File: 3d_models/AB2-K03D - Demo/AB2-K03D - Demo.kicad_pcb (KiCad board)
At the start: 2 copper layers, 209 parts

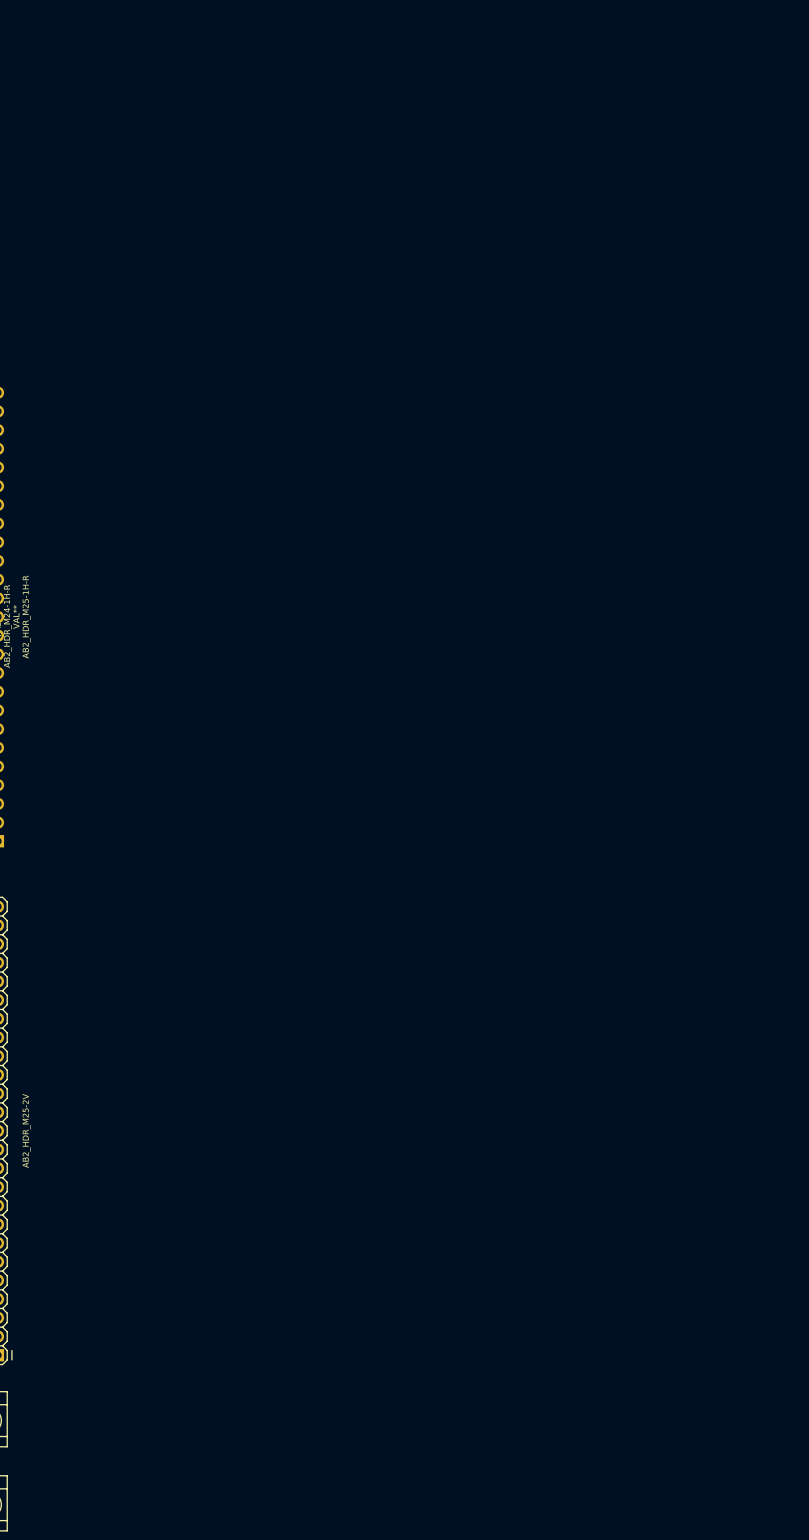
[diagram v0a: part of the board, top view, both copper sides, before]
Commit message: AB2-K03D: add FR4 substrates
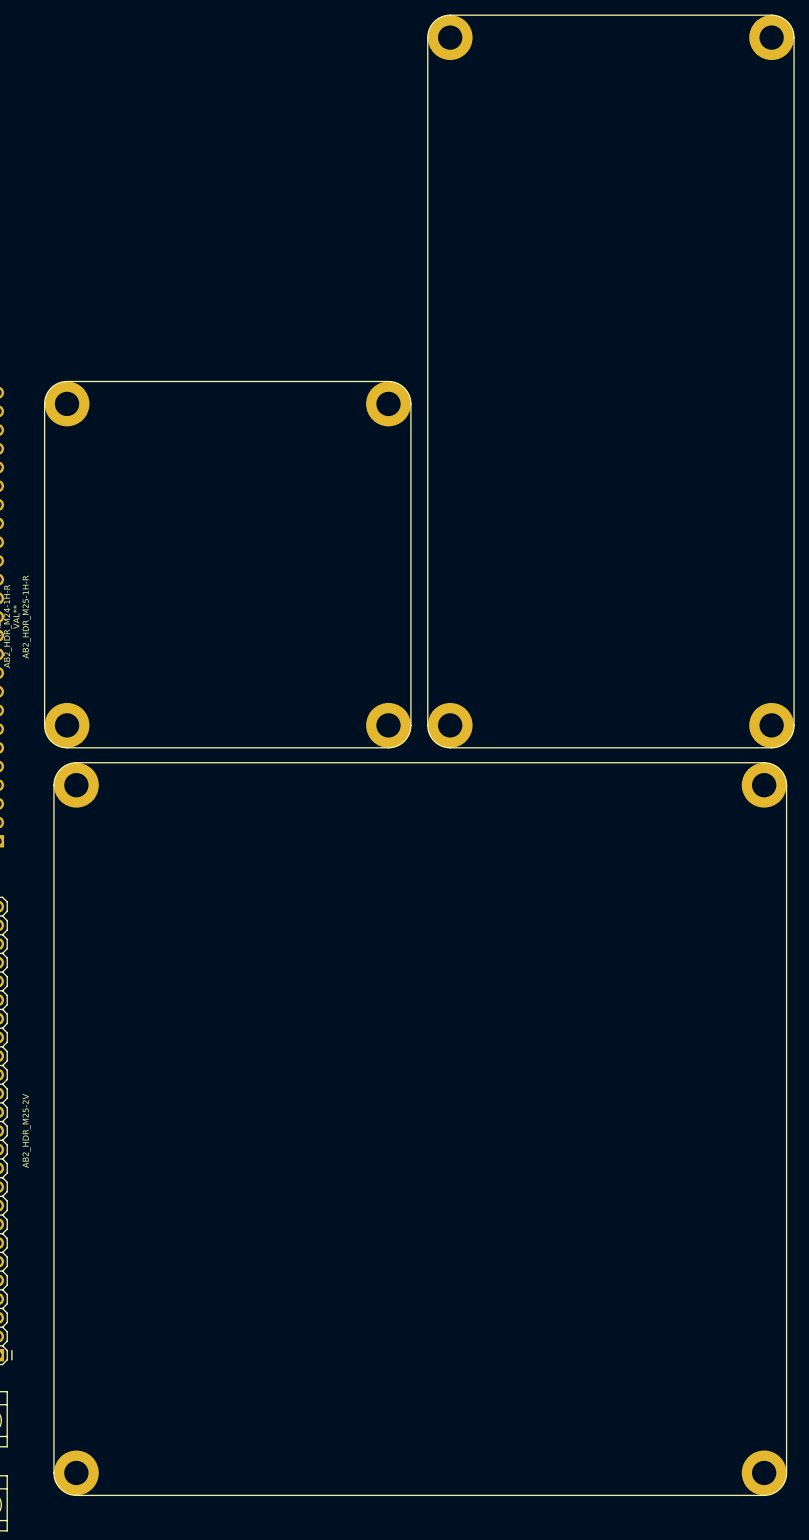
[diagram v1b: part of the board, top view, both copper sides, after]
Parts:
- added AB2_STANDOFF_1.96x1.96_BOARD_ROUNDED_CORNERS_KEEPOUT_FR4: VAL**, AB2_STANDOFF_1.96x1.96_BOARD_ROUNDED_CORNERS_KEEPOUT_FR4, F.Cu at (304.8, 166.4)
- added AB2_STANDOFF_1.96x3.92_BOARD_ROUNDED_CORNERS_KEEPOUT_FR4: VAL**, AB2_STANDOFF_1.96x3.92_BOARD_ROUNDED_CORNERS_KEEPOUT_FR4, F.Cu at (356.9, 166.4)
- added AB2_STANDOFF_3.92x3.92_BOARD_ROUNDED_CORNERS_KEEPOUT_FR4: VAL**, AB2_STANDOFF_3.92x3.92_BOARD_ROUNDED_CORNERS_KEEPOUT_FR4, F.Cu at (306.1, 268.0)
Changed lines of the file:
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@@
     (tracks 0)
     (zones 0)
-    (modules 209)
+    (modules 212)
     (nets 6)
   )
@@
       (at (xyz 0 0 0))
       (scale (xyz 0.3937 0.3937 0.3937))
+      (rotate (xyz 0 0 0))
+    )
+  )
+  (module AB2_STANDOFF_1.96x1.96_BOARD_ROUNDED_CORNERS_KEEPOUT_FR4 (layer F.Cu)
+    (at 304.8 166.37)
+    (fp_text reference AB2_STANDOFF_1.96x1.96_BOARD_ROUNDED_CORNERS_KEEPOUT_FR4 (at 24.892 -26.162) (layer F.SilkS) hide
+      (effects (font (size 0.8128 0.8128) (thickness 0.0762)))
+    )
+    (fp_text value VAL** (at 24.892 -23.622) (layer F.SilkS) hide
+      (effects (font (size 0.8128 0.8128) (thickness 0.0762)))
+    )
+    (fp_line (start 3.048 -49.784) (end 46.736 -49.784) (layer F.SilkS) (width 0.127))
+    (fp_line (start 0 -3.048) (end 0 -46.736) (layer F.SilkS) (width 0.127))
+    (fp_line (start 46.736 0) (end 3.048 0) (layer F.SilkS) (width 0.127))
+    (fp_line (start 49.784 -46.736) (end 49.784 -3.048) (layer F.SilkS) (width 0.127))
+    (fp_arc (start 3.048 -3.048) (end 3.048 0) (angle 90) (layer F.SilkS) (width 0.127))
+    (fp_arc (start 46.736 -3.048) (end 49.784 -3.048) (angle 90) (layer F.SilkS) (width 0.127))
+    (fp_arc (start 46.736 -46.736) (end 46.736 -49.784) (angle 90) (layer F.SilkS) (width 0.127))
+    (fp_arc (start 3.048 -46.736) (end 0 -46.736) (angle 90) (layer F.SilkS) (width 0.127))
+    (pad 1 thru_hole circle (at 3.048 -3.048) (size 6.096 6.096) (drill 3.302)
+      (layers *.Cu *.Mask F.SilkS)
+    )
+    (pad 1 thru_hole circle (at 46.736 -3.048) (size 6.096 6.096) (drill 3.302)
+      (layers *.Cu *.Mask F.SilkS)
+    )
+    (pad 1 thru_hole circle (at 46.736 -46.736) (size 6.096 6.096) (drill 3.302)
+      (layers *.Cu *.Mask F.SilkS)
+    )
+    (pad 1 thru_hole circle (at 3.048 -46.736) (size 6.096 6.096) (drill 3.302)
+      (layers *.Cu *.Mask F.SilkS)
+    )
+    (model ../3d_models/ab2_holesnpoles/AB2_FR4_1.96x1.96INx1.6MM_ROUNDED.wrl
+      (at (xyz 0 0 0))
+      (scale (xyz 0.3937 0.3937 0.3937))
+      (rotate (xyz 0 0 0))
+    )
+  )
+  (module AB2_STANDOFF_1.96x3.92_BOARD_ROUNDED_CORNERS_KEEPOUT_FR4 (layer F.Cu)
+    (at 356.87 166.37)
+    (fp_text reference AB2_STANDOFF_1.96x3.92_BOARD_ROUNDED_CORNERS_KEEPOUT_FR4 (at 24.892 -51.054) (layer F.SilkS) hide
+      (effects (font (size 0.8128 0.8128) (thickness 0.0762)))
+    )
+    (fp_text value VAL** (at 24.892 -48.514) (layer F.SilkS) hide
+      (effects (font (size 0.8128 0.8128) (thickness 0.0762)))
+    )
+    (fp_line (start 3.048 0) (end 46.736 0) (layer F.SilkS) (width 0.127))
+    (fp_line (start 3.048 -99.568) (end 46.736 -99.568) (layer F.SilkS) (width 0.127))
+    (fp_line (start 0 -3.048) (end 0 -96.52) (layer F.SilkS) (width 0.127))
+    (fp_line (start 49.784 -96.52) (end 49.784 -3.048) (layer F.SilkS) (width 0.127))
+    (fp_arc (start 3.048 -3.048) (end 3.048 0) (angle 90) (layer F.SilkS) (width 0.127))
+    (fp_arc (start 46.736 -3.048) (end 49.784 -3.048) (angle 90) (layer F.SilkS) (width 0.127))
+    (fp_arc (start 46.736 -96.52) (end 46.736 -99.568) (angle 90) (layer F.SilkS) (width 0.127))
+    (fp_arc (start 3.048 -96.52) (end 0 -96.52) (angle 90) (layer F.SilkS) (width 0.127))
+    (pad 1 thru_hole circle (at 3.048 -3.048) (size 6.096 6.096) (drill 3.302)
+      (layers *.Cu *.Mask F.SilkS)
+    )
+    (pad 1 thru_hole circle (at 46.736 -3.048) (size 6.096 6.096) (drill 3.302)
+      (layers *.Cu *.Mask F.SilkS)
+    )
+    (pad 1 thru_hole circle (at 46.736 -96.52) (size 6.096 6.096) (drill 3.302)
+      (layers *.Cu *.Mask F.SilkS)
+    )
+    (pad 1 thru_hole circle (at 3.048 -96.52) (size 6.096 6.096) (drill 3.302)
+      (layers *.Cu *.Mask F.SilkS)
+    )
+    (model ../3d_models/ab2_holesnpoles/AB2_FR4_1.96x3.92INx1.6MM_ROUNDED.wrl
+      (at (xyz 0 0 0))
+      (scale (xyz 0.3937 0.3937 0.3937))
+      (rotate (xyz 0 0 0))
+    )
+  )
+  (module AB2_STANDOFF_3.92x3.92_BOARD_ROUNDED_CORNERS_KEEPOUT_FR4 (layer F.Cu)
+    (at 306.07 267.97)
+    (fp_text reference AB2_STANDOFF_3.92x3.92_BOARD_ROUNDED_CORNERS_KEEPOUT_FR4 (at 49.784 -51.054) (layer F.SilkS) hide
+      (effects (font (size 0.8128 0.8128) (thickness 0.0762)))
+    )
+    (fp_text value VAL** (at 49.784 -48.514) (layer F.SilkS) hide
+      (effects (font (size 0.8128 0.8128) (thickness 0.0762)))
+    )
+    (fp_line (start 0 -3.048) (end 0 -96.52) (layer F.SilkS) (width 0.127))
+    (fp_line (start 96.52 0) (end 3.048 0) (layer F.SilkS) (width 0.127))
+    (fp_line (start 99.568 -96.52) (end 99.568 -3.048) (layer F.SilkS) (width 0.127))
+    (fp_line (start 3.048 -99.568) (end 96.52 -99.568) (layer F.SilkS) (width 0.127))
+    (fp_arc (start 3.048 -3.048) (end 3.048 0) (angle 90) (layer F.SilkS) (width 0.127))
+    (fp_arc (start 96.52 -3.048) (end 99.568 -3.048) (angle 90) (layer F.SilkS) (width 0.127))
+    (fp_arc (start 96.52 -96.52) (end 96.52 -99.568) (angle 90) (layer F.SilkS) (width 0.127))
+    (fp_arc (start 3.048 -96.52) (end 0 -96.52) (angle 90) (layer F.SilkS) (width 0.127))
+    (pad 1 thru_hole circle (at 3.048 -3.048) (size 6.096 6.096) (drill 3.302)
+      (layers *.Cu *.Mask F.SilkS)
+    )
+    (pad 1 thru_hole circle (at 96.52 -3.048) (size 6.096 6.096) (drill 3.302)
+      (layers *.Cu *.Mask F.SilkS)
+    )
+    (pad 1 thru_hole circle (at 96.52 -96.52) (size 6.096 6.096) (drill 3.302)
+      (layers *.Cu *.Mask F.SilkS)
+    )
+    (pad 1 thru_hole circle (at 3.048 -96.52) (size 6.096 6.096) (drill 3.302)
+      (layers *.Cu *.Mask F.SilkS)
+    )
+    (model ../3d_models/ab2_holesnpoles/AB2_FR4_3.92x3.92INx1.6MM_ROUNDED.wrl
+      (at (xyz 0 0 0))
+      (scale (xyz 0.3937 0.3937 0.3937))
